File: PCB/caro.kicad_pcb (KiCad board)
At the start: 2 copper layers, 83.8 x 33 mm, 11 parts, among them SW1 Control Button, SW2 Power Switch, U1 DFR0299

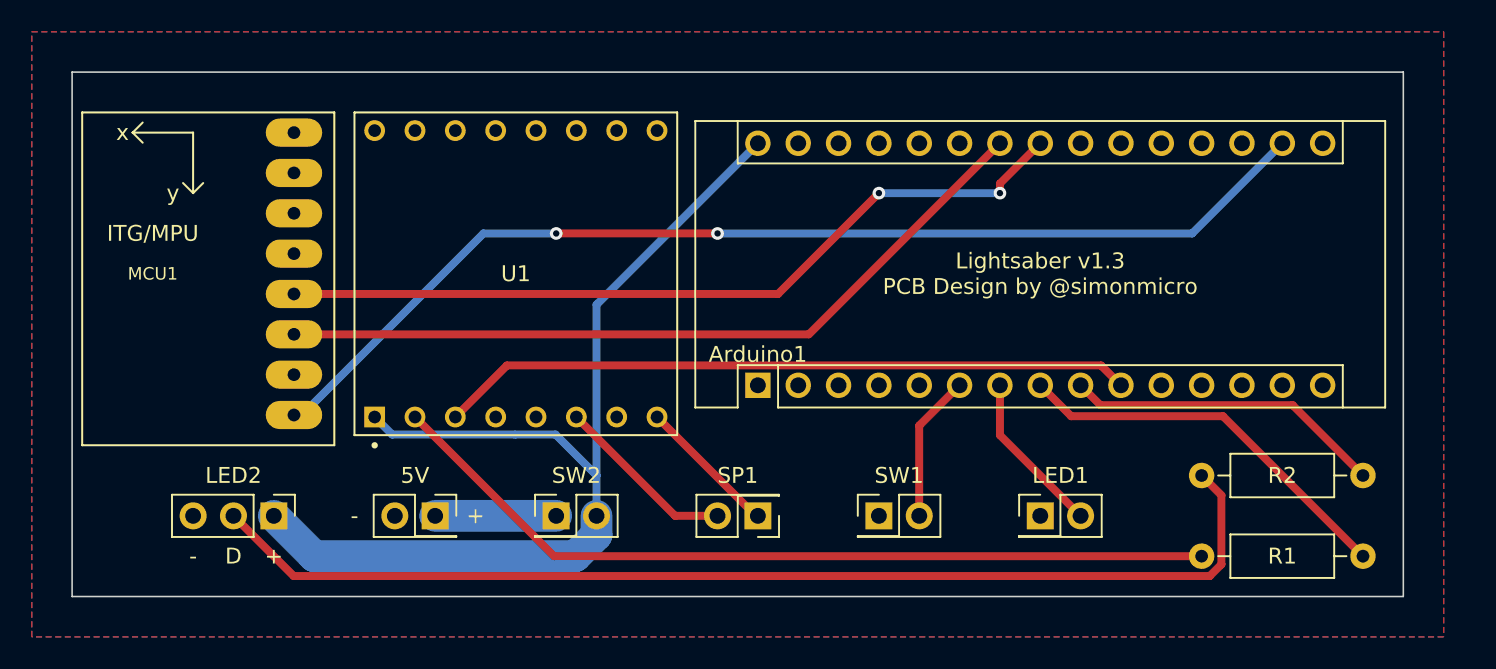
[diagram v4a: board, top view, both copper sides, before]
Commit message: Revision v1.4 Swapped MCU and SDCard
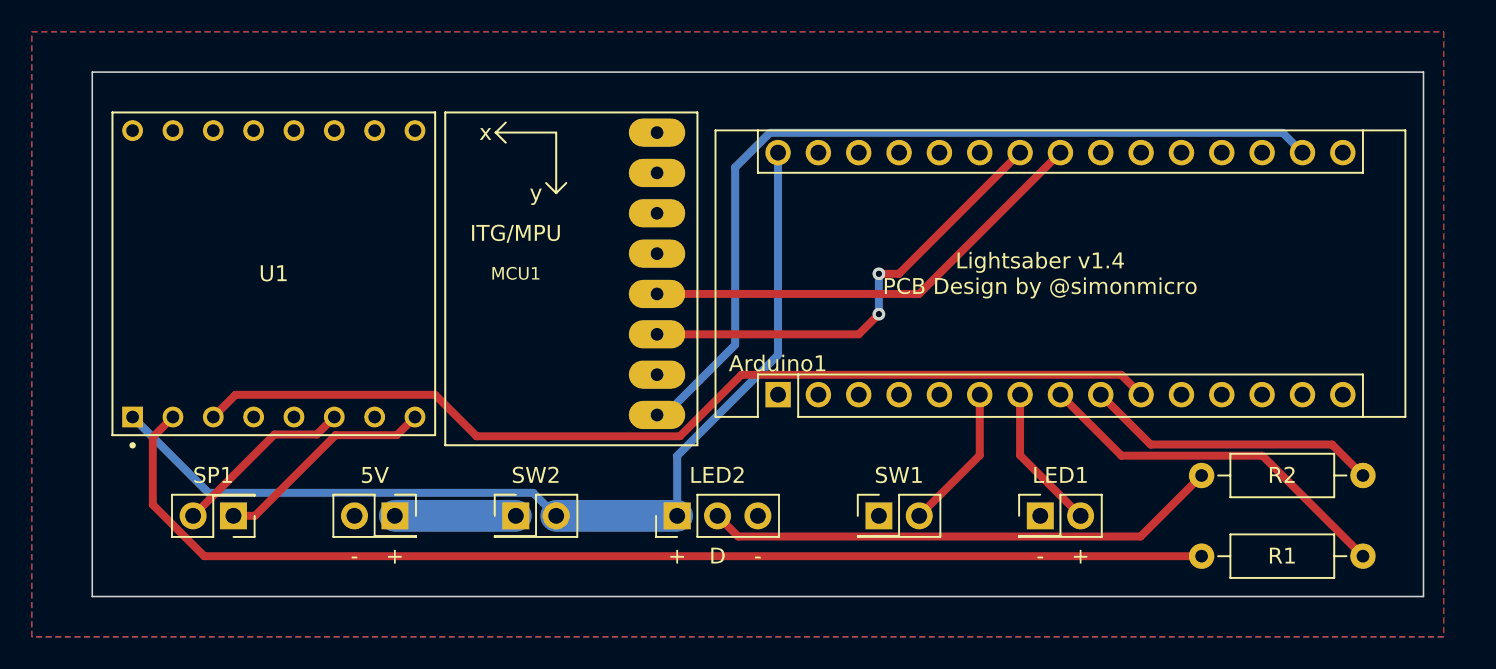
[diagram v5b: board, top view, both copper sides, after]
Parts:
- moved SP1 33.0 mm to (114.3, 109.2)
- moved LED2 25.4 mm to (142.2, 109.2), turned to 90 degrees
- moved MCU1 22.9 mm to (132.1, 94.0)
- moved U1 15.2 mm to (116.8, 94.0)
- moved 5V 2.54 mm to (124.5, 109.2)
- moved SW2 2.54 mm to (132.1, 109.2)
- moved Arduino1 1.40 mm to (148.6, 101.6)
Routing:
- net Net-(LED2-Pad4): track 70.2 -> 32.6 mm
- net A4: track 51.3 -> 29.1 mm, vias 2 -> 0
- net A5: track 49.4 -> 29.1 mm, vias 0 -> 2
- net Net-(R1-Pad2): track 53.2 -> 73.4 mm
- net D7: track 43.8 -> 62.2 mm
- net 3.3V: track 69.3 -> 55.1 mm, vias 2 -> 0
- net Net-(SP1-Pad1): track 8.93 -> 14.0 mm
- net 5V: track 66.3 -> 62.4 mm
- net D6: track 20.1 -> 18.6 mm
- net D5: track 24.8 -> 23.3 mm
- net D4: track 10.3 -> 9.21 mm
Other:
- board text added: "Lightsaber v1.4 PCB Design by @simonmicro"
- board text removed: "Lightsaber v1.3 PCB Design by @simonmicro"

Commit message: Moved resistor to increase distance to HIGH_PWR tracks
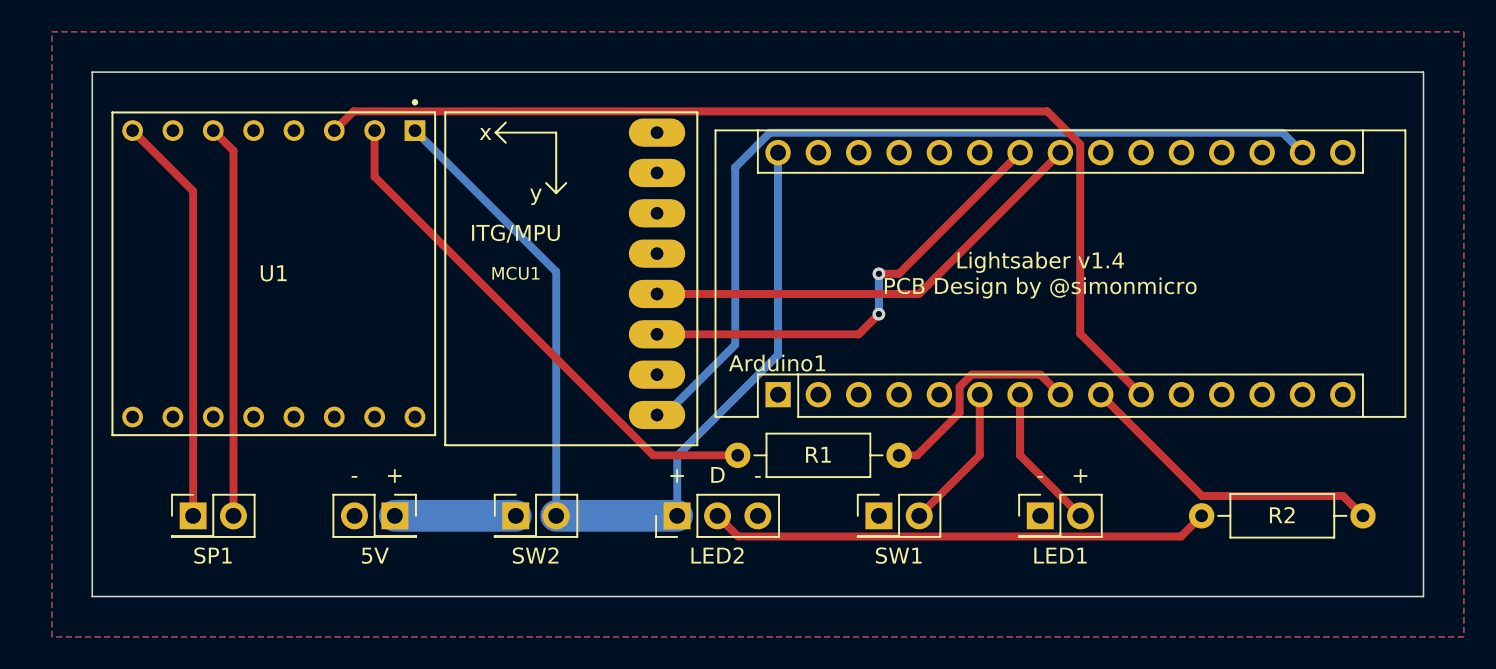
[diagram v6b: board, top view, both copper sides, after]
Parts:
- moved R1 29.9 mm to (156.2, 105.4)
- moved R2 2.54 mm to (185.4, 109.2)
- moved SP1 2.54 mm to (111.8, 109.2), turned to 0 degrees
- turned U1 to -90 degrees
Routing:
- net Net-(R1-Pad2): track 73.4 -> 33.0 mm
- net Net-(SP1-Pad2): track 11.5 -> 24.8 mm
- net Net-(SP1-Pad1): track 14.0 -> 25.8 mm
- net D5: track 23.3 -> 13.7 mm
- net D7: track 62.2 -> 65.7 mm
- net 5V: track 62.4 -> 61.1 mm
- net D6: track 18.6 -> 19.7 mm
- net Net-(LED2-Pad4): track 32.6 -> 31.6 mm

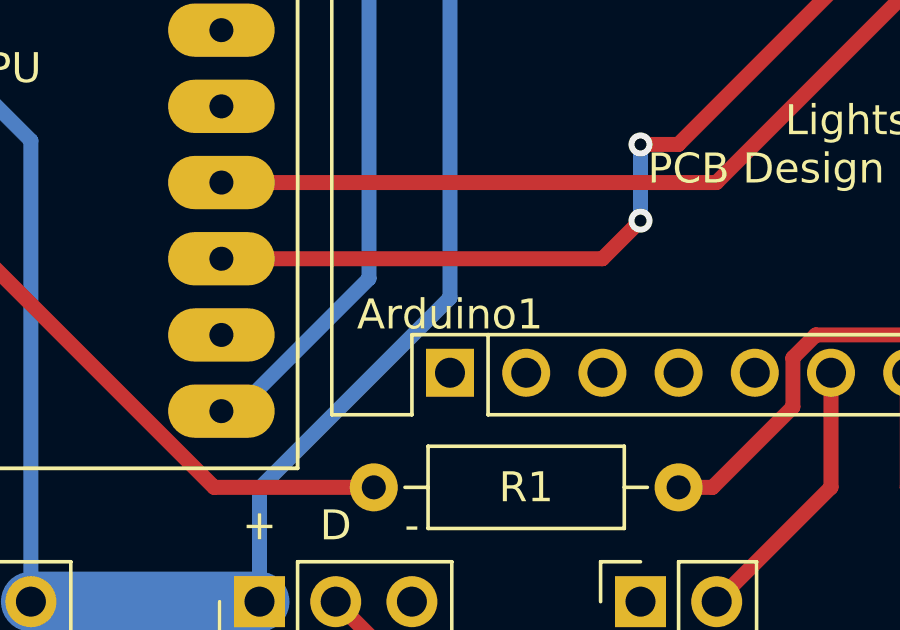
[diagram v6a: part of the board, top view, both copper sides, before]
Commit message: Corrected worng annotation
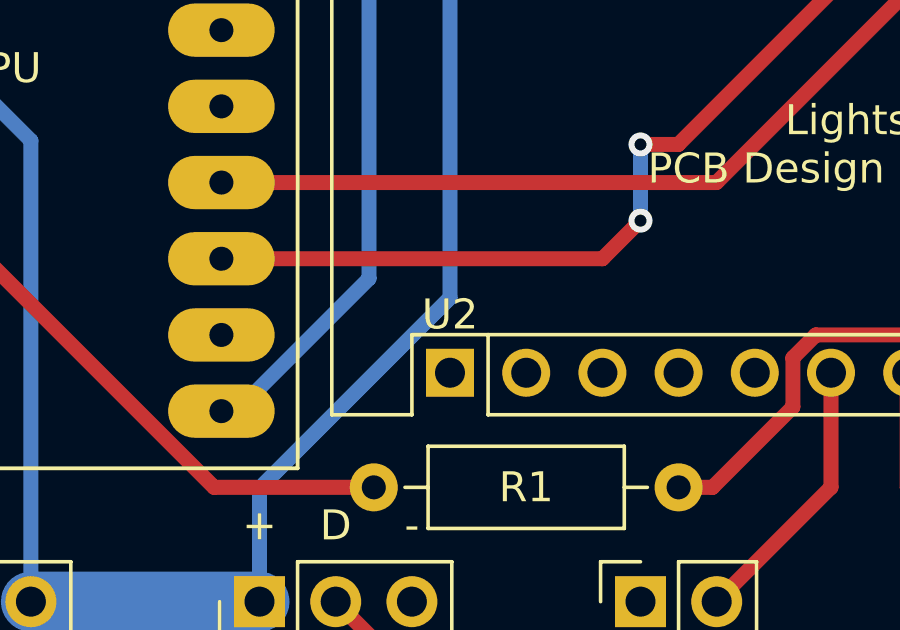
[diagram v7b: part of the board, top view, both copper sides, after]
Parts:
- renumbered Arduino1 to U2
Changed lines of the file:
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@@
   (net 8 "D6")
   (net 9 "D7")
-  (net 10 "unconnected-(Arduino1-Pad1)")
-  (net 11 "unconnected-(Arduino1-Pad2)")
-  (net 12 "unconnected-(Arduino1-Pad3)")
-  (net 13 "unconnected-(Arduino1-Pad5)")
+  (net 10 "unconnected-(U2-Pad1)")
+  (net 11 "unconnected-(U2-Pad2)")
+  (net 12 "unconnected-(U2-Pad3)")
+  (net 13 "unconnected-(U2-Pad5)")
   (net 14 "5V")
-  (net 15 "unconnected-(Arduino1-Pad11)")
-  (net 16 "unconnected-(Arduino1-Pad12)")
-  (net 17 "unconnected-(Arduino1-Pad13)")
-  (net 18 "unconnected-(Arduino1-Pad14)")
-  (net 19 "unconnected-(Arduino1-Pad15)")
-  (net 20 "unconnected-(Arduino1-Pad16)")
-  (net 21 "unconnected-(Arduino1-Pad18)")
-  (net 22 "unconnected-(Arduino1-Pad19)")
-  (net 23 "unconnected-(Arduino1-Pad20)")
-  (net 24 "unconnected-(Arduino1-Pad21)")
-  (net 25 "unconnected-(Arduino1-Pad22)")
-  (net 26 "unconnected-(Arduino1-Pad25)")
-  (net 27 "unconnected-(Arduino1-Pad26)")
-  (net 28 "unconnected-(Arduino1-Pad27)")
-  (net 29 "unconnected-(Arduino1-Pad28)")
+  (net 15 "unconnected-(U2-Pad11)")
+  (net 16 "unconnected-(U2-Pad12)")
+  (net 17 "unconnected-(U2-Pad13)")
+  (net 18 "unconnected-(U2-Pad14)")
+  (net 19 "unconnected-(U2-Pad15)")
+  (net 20 "unconnected-(U2-Pad16)")
+  (net 21 "unconnected-(U2-Pad18)")
+  (net 22 "unconnected-(U2-Pad19)")
+  (net 23 "unconnected-(U2-Pad20)")
+  (net 24 "unconnected-(U2-Pad21)")
+  (net 25 "unconnected-(U2-Pad22)")
+  (net 26 "unconnected-(U2-Pad25)")
+  (net 27 "unconnected-(U2-Pad26)")
+  (net 28 "unconnected-(U2-Pad27)")
+  (net 29 "unconnected-(U2-Pad28)")
   (net 30 "+5V")
   (net 31 "Net-(R1-Pad2)")
@@
     (property "Sheetname" "")
     (attr through_hole)
-    (fp_text reference "Arduino1" (at 1.94 0 180) (layer "F.SilkS")
+    (fp_text reference "U2" (at 1.94 0 180) (layer "F.SilkS")
       (effects (font (size 1 1) (thickness 0.15)))
     )
@@
     (fp_line (start 16.51 39.37) (end -1.27 39.37) (layer "F.Fab") (width 0.1))
     (pad "1" thru_hole rect locked (at 0 0 90) (size 1.6 1.6) (drill 1) (layers *.Cu *.Mask)
-      (net 10 "unconnected-(Arduino1-Pad1)") (pinfunction "D1/TX") (pintype "bidirectional"))
+      (net 10 "unconnected-(U2-Pad1)") (pinfunction "D1/TX") (pintype "bidirectional"))
     (pad "2" thru_hole oval locked (at 0 2.54 90) (size 1.6 1.6) (drill 1) (layers *.Cu *.Mask)
-      (net 11 "unconnected-(Arduino1-Pad2)") (pinfunction "D0/RX") (pintype "bidirectional"))
+      (net 11 "unconnected-(U2-Pad2)") (pinfunction "D0/RX") (pintype "bidirectional"))
     (pad "3" thru_hole oval locked (at 0 5.08 90) (size 1.6 1.6) (drill 1) (layers *.Cu *.Mask)
-      (net 12 "unconnected-(Arduino1-Pad3)") (pinfunction "~{RESET}") (pintype "input"))
+      (net 12 "unconnected-(U2-Pad3)") (pinfunction "~{RESET}") (pintype "input"))
     (pad "4" thru_hole oval locked (at 0 7.62 90) (size 1.6 1.6) (drill 1) (layers *.Cu *.Mask)
       (net 2 "GND") (pinfunction "GND") (pintype "power_in"))
     (pad "5" thru_hole oval locked (at 0 10.16 90) (size 1.6 1.6) (drill 1) (layers *.Cu *.Mask)
-      (net 13 "unconnected-(Arduino1-Pad5)") (pinfunction "D2") (pintype "bidirectional"))
+      (net 13 "unconnected-(U2-Pad5)") (pinfunction "D2") (pintype "bidirectional"))
     (pad "6" thru_hole oval locked (at 0 12.7 90) (size 1.6 1.6) (drill 1) (layers *.Cu *.Mask)
       (net 3 "D3") (pinfunction "D3") (pintype "bidirectional"))
@@
       (net 9 "D7") (pinfunction "D7") (pintype "bidirectional"))
     (pad "11" thru_hole oval locked (at 0 25.4 90) (size 1.6 1.6) (drill 1) (layers *.Cu *.Mask)
-      (net 15 "unconnected-(Arduino1-Pad11)") (pinfunction "D8") (pintype "bidirectional"))
+      (net 15 "unconnected-(U2-Pad11)") (pinfunction "D8") (pintype "bidirectional"))
     (pad "12" thru_hole oval locked (at 0 27.94 90) (size 1.6 1.6) (drill 1) (layers *.Cu *.Mask)
-      (net 16 "unconnected-(Arduino1-Pad12)") (pinfunction "D9") (pintype "bidirectional"))
+      (net 16 "unconnected-(U2-Pad12)") (pinfunction "D9") (pintype "bidirectional"))
     (pad "13" thru_hole oval locked (at 0 30.48 90) (size 1.6 1.6) (drill 1) (layers *.Cu *.Mask)
-      (net 17 "unconnected-(Arduino1-Pad13)") (pinfunction "D10") (pintype "bidirectional"))
+      (net 17 "unconnected-(U2-Pad13)") (pinfunction "D10") (pintype "bidirectional"))
     (pad "14" thru_hole oval locked (at 0 33.02 90) (size 1.6 1.6) (drill 1) (layers *.Cu *.Mask)
-      (net 18 "unconnected-(Arduino1-Pad14)") (pinfunction "D11") (pintype "bidirectional"))
+      (net 18 "unconnected-(U2-Pad14)") (pinfunction "D11") (pintype "bidirectional"))
     (pad "15" thru_hole oval locked (at 0 35.56 90) (size 1.6 1.6) (drill 1) (layers *.Cu *.Mask)
-      (net 19 "unconnected-(Arduino1-Pad15)") (pinfunction "D12") (pintype "bidirectional"))
+      (net 19 "unconnected-(U2-Pad15)") (pinfunction "D12") (pintype "bidirectional"))
     (pad "16" thru_hole oval locked (at 15.24 35.56 90) (size 1.6 1.6) (drill 1) (layers *.Cu *.Mask)
-      (net 20 "unconnected-(Arduino1-Pad16)") (pinfunction "D13") (pintype "bidirectional"))
+      (net 20 "unconnected-(U2-Pad16)") (pinfunction "D13") (pintype "bidirectional"))
     (pad "17" thru_hole oval locked (at 15.24 33.02 90) (size 1.6 1.6) (drill 1) (layers *.Cu *.Mask)
       (net 1 "3.3V") (pinfunction "3V3") (pintype "power_out"))
     (pad "18" thru_hole oval locked (at 15.24 30.48 90) (size 1.6 1.6) (drill 1) (layers *.Cu *.Mask)
-      (net 21 "unconnected-(Arduino1-Pad18)") (pinfunction "AREF") (pintype "input"))
+      (net 21 "unconnected-(U2-Pad18)") (pinfunction "AREF") (pintype "input"))
     (pad "19" thru_hole oval locked (at 15.24 27.94 90) (size 1.6 1.6) (drill 1) (layers *.Cu *.Mask)
-      (net 22 "unconnected-(Arduino1-Pad19)") (pinfunction "A0") (pintype "bidirectional"))
+      (net 22 "unconnected-(U2-Pad19)") (pinfunction "A0") (pintype "bidirectional"))
     (pad "20" thru_hole oval locked (at 15.24 25.4 90) (size 1.6 1.6) (drill 1) (layers *.Cu *.Mask)
-      (net 23 "unconnected-(Arduino1-Pad20)") (pinfunction "A1") (pintype "bidirectional"))
+      (net 23 "unconnected-(U2-Pad20)") (pinfunction "A1") (pintype "bidirectional"))
     (pad "21" thru_hole oval locked (at 15.24 22.86 90) (size 1.6 1.6) (drill 1) (layers *.Cu *.Mask)
-      (net 24 "unconnected-(Arduino1-Pad21)") (pinfunction "A2") (pintype "bidirectional"))
+      (net 24 "unconnected-(U2-Pad21)") (pinfunction "A2") (pintype "bidirectional"))
     (pad "22" thru_hole oval locked (at 15.24 20.32 90) (size 1.6 1.6) (drill 1) (layers *.Cu *.Mask)
-      (net 25 "unconnected-(Arduino1-Pad22)") (pinfunction "A3") (pintype "bidirectional"))
+      (net 25 "unconnected-(U2-Pad22)") (pinfunction "A3") (pintype "bidirectional"))
     (pad "23" thru_hole oval locked (at 15.24 17.78 90) (size 1.6 1.6) (drill 1) (layers *.Cu *.Mask)
       (net 5 "A4") (pinfunction "A4") (pintype "bidirectional"))
@@
       (net 7 "A5") (pinfunction "A5") (pintype "bidirectional"))
     (pad "25" thru_hole oval locked (at 15.24 12.7 90) (size 1.6 1.6) (drill 1) (layers *.Cu *.Mask)
-      (net 26 "unconnected-(Arduino1-Pad25)") (pinfunction "A6") (pintype "bidirectional"))
+      (net 26 "unconnected-(U2-Pad25)") (pinfunction "A6") (pintype "bidirectional"))
     (pad "26" thru_hole oval locked (at 15.24 10.16 90) (size 1.6 1.6) (drill 1) (layers *.Cu *.Mask)
-      (net 27 "unconnected-(Arduino1-Pad26)") (pinfunction "A7") (pintype "bidirectional"))
+      (net 27 "unconnected-(U2-Pad26)") (pinfunction "A7") (pintype "bidirectional"))
     (pad "27" thru_hole oval locked (at 15.24 7.62 90) (size 1.6 1.6) (drill 1) (layers *.Cu *.Mask)
-      (net 28 "unconnected-(Arduino1-Pad27)") (pinfunction "+5V") (pintype "power_out"))
+      (net 28 "unconnected-(U2-Pad27)") (pinfunction "+5V") (pintype "power_out"))
     (pad "28" thru_hole oval locked (at 15.24 5.08 90) (size 1.6 1.6) (drill 1) (layers *.Cu *.Mask)
-      (net 29 "unconnected-(Arduino1-Pad28)") (pinfunction "~{RESET}") (pintype "input"))
+      (net 29 "unconnected-(U2-Pad28)") (pinfunction "~{RESET}") (pintype "input"))
     (pad "29" thru_hole oval locked (at 15.24 2.54 90) (size 1.6 1.6) (drill 1) (layers *.Cu *.Mask)
       (net 2 "GND") (pinfunction "GND") (pintype "power_in"))
